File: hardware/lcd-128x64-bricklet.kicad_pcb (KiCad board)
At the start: 2 copper layers, 95 x 55 mm, 44 parts, among them P1 CON-SENSOR2, P2 Debug, P3 BOOT, P4 CON_4Wire_ER-TP028-1, Q1 2N7002, U1 XMC130024, U2 TSC2046E, U3 LCD-ERC12864, U4 DRILL, U5 DRILL, U6 DRILL, U7 DRILL

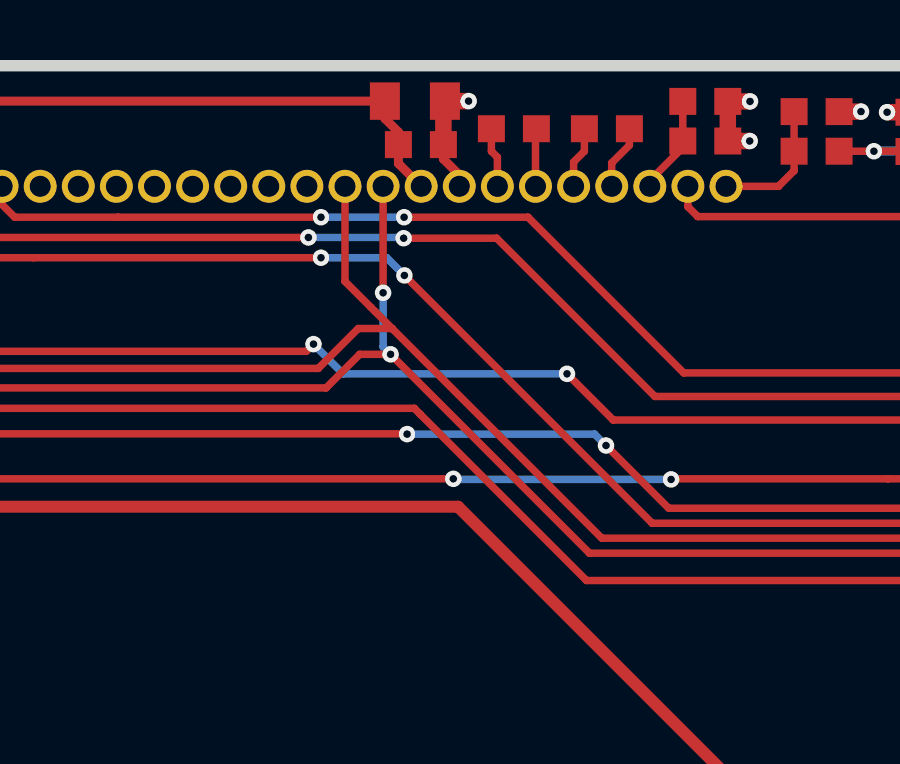
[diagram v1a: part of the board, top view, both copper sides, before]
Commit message: display has to be connected to MOSI (not MISO)
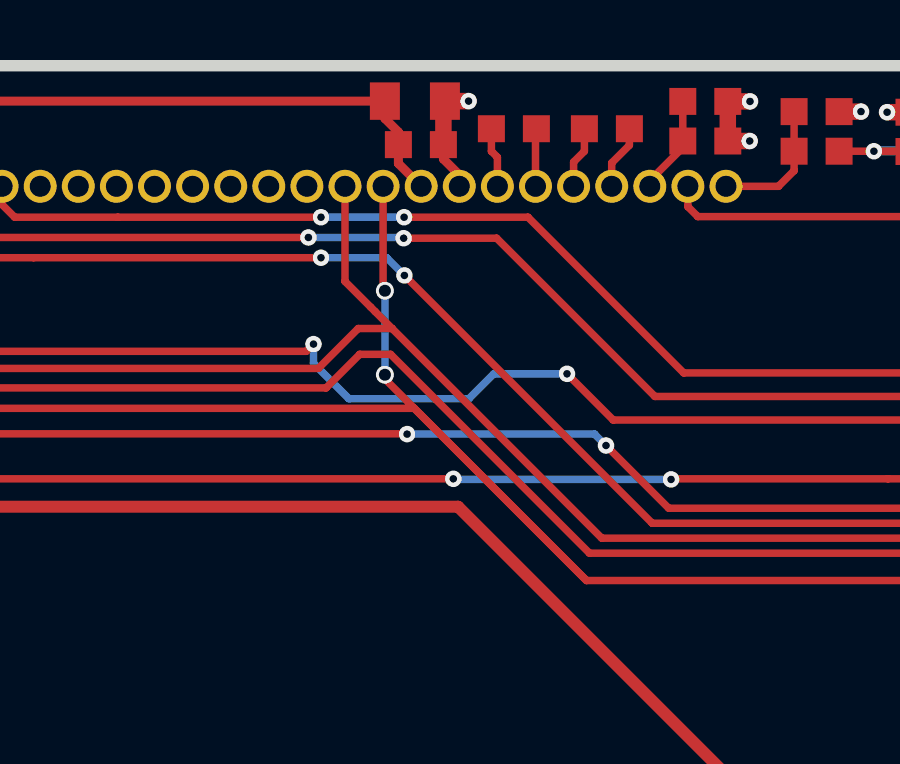
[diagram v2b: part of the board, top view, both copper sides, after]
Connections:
- P1 pad 1: Net-(P1-Pad1) -> (no net)
- U1 pad 3: Net-(U1-Pad3) -> (no net)
- U1 pad 5: Net-(U1-Pad5) -> (no net)
- U1 pad 6: Net-(U1-Pad6) -> (no net)
- U1 pad 8: Net-(U1-Pad8) -> (no net)
- U2 pad 8: Net-(U2-Pad8) -> (no net)
- U2 pad 9: Net-(U2-Pad9) -> (no net)
- U3 pad 13: M-MISO -> M-MOSI
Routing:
- net M-MOSI: track 77.5 -> 93.4 mm, vias 2 -> 4
- net M-MISO: track 83.1 -> 77.3 mm, vias 2 -> 0
- net TS-BUSY: track 78.5 -> 79.5 mm
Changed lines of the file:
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@@
-(kicad_pcb (version 4) (host pcbnew 4.0.2+dfsg1-stable)
+(kicad_pcb (version 4) (host pcbnew 4.0.7-e2-6376~58~ubuntu17.04.1)
   (general
     (links 100)
     (no_connects 0)
-    (area 91.044999 60.444999 187.755001 117.155001)
+    (area 91.709499 61.109499 187.090501 116.490501)
     (thickness 1.6)
     (drawings 16)
-    (tracks 479)
+    (tracks 484)
     (zones 0)
     (modules 44)
-    (nets 51)
+    (nets 44)
   )
   (page A4)
@@
   )
   (setup
-    (last_trace_width 0.2)
+    (last_trace_width 0.25)
     (user_trace_width 0.2)
     (user_trace_width 0.25)
@@
   (net 42 "Net-(D2-Pad2)")
   (net 43 "Net-(R8-Pad1)")
-  (net 44 "Net-(P1-Pad1)")
-  (net 45 "Net-(U1-Pad3)")
-  (net 46 "Net-(U1-Pad5)")
-  (net 47 "Net-(U1-Pad6)")
-  (net 48 "Net-(U1-Pad8)")
-  (net 49 "Net-(U2-Pad8)")
-  (net 50 "Net-(U2-Pad9)")
   (net_class Default "This is the default net class."
     (clearance 0.15)
@@
     (add_net "Net-(D1-Pad2)")
     (add_net "Net-(D2-Pad2)")
-    (add_net "Net-(P1-Pad1)")
     (add_net "Net-(P1-Pad4)")
     (add_net "Net-(P1-Pad5)")
@@
     (add_net "Net-(RP2-Pad7)")
     (add_net "Net-(RP2-Pad8)")
-    (add_net "Net-(U1-Pad3)")
-    (add_net "Net-(U1-Pad5)")
-    (add_net "Net-(U1-Pad6)")
-    (add_net "Net-(U1-Pad8)")
-    (add_net "Net-(U2-Pad8)")
-    (add_net "Net-(U2-Pad9)")
     (add_net PENIRQ)
     (add_net S-CLK)
@@
     (fp_line (start 6 -4.3) (end -6 -4.3) (layer F.Fab) (width 0.05))
     (fp_line (start -6 -4.3) (end -6 -0.25) (layer F.Fab) (width 0.05))
-    (pad 1 smd rect (at -3.75 -4.6 90) (size 0.6 1.8) (layers F.Cu F.Paste F.Mask)
-      (net 44 "Net-(P1-Pad1)"))
+    (pad 1 smd rect (at -3.75 -4.6 90) (size 0.6 1.8) (layers F.Cu F.Paste F.Mask))
     (pad 2 smd rect (at -2.5 -4.6 90) (size 0.6 1.8) (layers F.Cu F.Paste F.Mask)
       (net 1 GND))
@@
     (pad 2 smd oval (at -2.025 -0.75 180) (size 1 0.3) (layers F.Cu F.Paste F.Mask)
       (net 43 "Net-(R8-Pad1)"))
-    (pad 3 smd oval (at -2.025 -0.25 180) (size 1 0.3) (layers F.Cu F.Paste F.Mask)
-      (net 45 "Net-(U1-Pad3)"))
+    (pad 3 smd oval (at -2.025 -0.25 180) (size 1 0.3) (layers F.Cu F.Paste F.Mask))
     (pad 4 smd oval (at -2.025 0.25 180) (size 1 0.3) (layers F.Cu F.Paste F.Mask)
       (net 14 "Net-(P3-Pad2)"))
-    (pad 5 smd oval (at -2.025 0.75 180) (size 1 0.3) (layers F.Cu F.Paste F.Mask)
-      (net 46 "Net-(U1-Pad5)"))
-    (pad 6 smd oval (at -2.025 1.25 180) (size 1 0.3) (layers F.Cu F.Paste F.Mask)
-      (net 47 "Net-(U1-Pad6)"))
+    (pad 5 smd oval (at -2.025 0.75 180) (size 1 0.3) (layers F.Cu F.Paste F.Mask))
+    (pad 6 smd oval (at -2.025 1.25 180) (size 1 0.3) (layers F.Cu F.Paste F.Mask))
     (pad 7 smd oval (at -1.25 2.025 270) (size 1 0.3) (layers F.Cu F.Paste F.Mask)
       (net 21 "Net-(R1-Pad1)"))
-    (pad 8 smd oval (at -0.75 2.025 270) (size 1 0.3) (layers F.Cu F.Paste F.Mask)
-      (net 48 "Net-(U1-Pad8)"))
+    (pad 8 smd oval (at -0.75 2.025 270) (size 1 0.3) (layers F.Cu F.Paste F.Mask))
     (pad 9 smd oval (at -0.25 2.025 270) (size 1 0.3) (layers F.Cu F.Paste F.Mask)
       (net 1 GND))
@@
     (pad 7 smd rect (at 1.62306 2.97434 90) (size 0.4191 1.778) (layers F.Cu F.Paste F.Mask)
       (net 3 VCC))
-    (pad 8 smd rect (at 2.2733 2.97434 90) (size 0.4191 1.778) (layers F.Cu F.Paste F.Mask)
-      (net 49 "Net-(U2-Pad8)"))
-    (pad 9 smd rect (at 2.2733 -2.97434 270) (size 0.4191 1.778) (layers F.Cu F.Paste F.Mask)
-      (net 50 "Net-(U2-Pad9)"))
+    (pad 8 smd rect (at 2.2733 2.97434 90) (size 0.4191 1.778) (layers F.Cu F.Paste F.Mask))
+    (pad 9 smd rect (at 2.2733 -2.97434 270) (size 0.4191 1.778) (layers F.Cu F.Paste F.Mask))
     (pad 10 smd rect (at 1.62306 -2.97434 270) (size 0.4191 1.778) (layers F.Cu F.Paste F.Mask)
       (net 3 VCC))
@@
       (net 32 M-CLK))
     (pad 13 thru_hole circle (at 1.94 -25) (size 1.1 1.1) (drill 0.7) (layers *.Cu *.Mask F.SilkS)
-      (net 24 M-MISO))
+      (net 41 M-MOSI))
     (pad 14 thru_hole circle (at 3.21 -25) (size 1.1 1.1) (drill 0.7) (layers *.Cu *.Mask F.SilkS)
       (net 3 VCC))
@@
   (segment (start 175.275 77.5493) (end 173.38 77.5493) (width 0.25) (layer F.Cu) (net 24))
   (segment (start 173.38 77.5493) (end 148.2193 77.5493) (width 0.25) (layer F.Cu) (net 24))
-  (segment (start 141.34 68.87) (end 141.34 65.2) (width 0.25) (layer F.Cu) (net 24))
-  (via (at 141.34 68.87) (size 0.55) (drill 0.25) (layers F.Cu B.Cu) (net 24))
-  (segment (start 141.34 70.67) (end 141.34 68.87) (width 0.25) (layer B.Cu) (net 24))
-  (segment (start 141.59 70.92) (end 141.34 70.67) (width 0.25) (layer B.Cu) (net 24))
-  (via (at 141.59 70.92) (size 0.55) (drill 0.25) (layers F.Cu B.Cu) (net 24))
   (segment (start 148.2193 77.5493) (end 141.59 70.92) (width 0.25) (layer F.Cu) (net 24))
   (segment (start 181.075 73.6) (end 181.85 73.6) (width 0.2) (layer F.Cu) (net 25))
@@
   (segment (start 177.425 75.275) (end 175.325 75.275) (width 0.25) (layer F.Cu) (net 37))
   (segment (start 177.8 74.9) (end 177.425 75.275) (width 0.25) (layer F.Cu) (net 37))
+  (segment (start 147.47 71.57) (end 145.03 71.57) (width 0.25) (layer B.Cu) (net 38))
+  (segment (start 139.02 71.22) (end 139.02 70.58) (width 0.25) (layer B.Cu) (net 38))
+  (segment (start 140.2 72.4) (end 139.02 71.22) (width 0.25) (layer B.Cu) (net 38))
+  (segment (start 144.2 72.4) (end 140.2 72.4) (width 0.25) (layer B.Cu) (net 38))
+  (segment (start 145.03 71.57) (end 144.2 72.4) (width 0.25) (layer B.Cu) (net 38))
   (segment (start 101.62434 69.32742) (end 105.59742 69.32742) (width 0.25) (layer F.Cu) (net 38))
   (segment (start 176.12 73.1) (end 177.025 73.1) (width 0.25) (layer F.Cu) (net 38))
@@
   (segment (start 147.47 71.57) (end 149.01 73.11) (width 0.25) (layer F.Cu) (net 38))
   (via (at 147.47 71.57) (size 0.55) (drill 0.25) (layers F.Cu B.Cu) (net 38))
-  (segment (start 140.01 71.57) (end 147.47 71.57) (width 0.25) (layer B.Cu) (net 38))
-  (segment (start 139.02 70.58) (end 140.01 71.57) (width 0.25) (layer B.Cu) (net 38))
   (via (at 139.02 70.58) (size 0.55) (drill 0.25) (layers F.Cu B.Cu) (net 38))
   (segment (start 138.78 70.82) (end 139.02 70.58) (width 0.25) (layer F.Cu) (net 38))
@@
   (segment (start 173.74 72.53) (end 172.76 71.55) (width 0.25) (layer B.Cu) (net 40))
   (via (at 173.74 72.53) (size 0.55) (drill 0.25) (layers F.Cu B.Cu) (net 40))
+  (segment (start 141.4 71.6) (end 141.4 71.74) (width 0.25) (layer F.Cu) (net 41))
+  (segment (start 141.4 71.74) (end 148.12 78.46) (width 0.25) (layer F.Cu) (net 41))
+  (segment (start 141.34 65.32) (end 141.34 68.74) (width 0.25) (layer F.Cu) (net 41))
+  (via (at 141.4 71.6) (size 0.6) (drill 0.4) (layers F.Cu B.Cu) (net 41))
+  (segment (start 141.4 68.8) (end 141.4 71.6) (width 0.25) (layer B.Cu) (net 41))
+  (via (at 141.4 68.8) (size 0.6) (drill 0.4) (layers F.Cu B.Cu) (net 41))
+  (segment (start 141.34 68.74) (end 141.4 68.8) (width 0.25) (layer F.Cu) (net 41))
   (segment (start 175.36 78.46) (end 148.12 78.46) (width 0.25) (layer F.Cu) (net 41))
   (segment (start 106.60718 68.69718) (end 101.92434 68.69718) (width 0.25) (layer F.Cu) (net 41))
